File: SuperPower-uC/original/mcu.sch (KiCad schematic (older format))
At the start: 43 parts, among them J7 mcu_pinout, J8 mcu_pinout, Q7 S8050, Q8 S8050, U6 CP2102N-A01-GQFN28, U7 ESP32-WROOM32

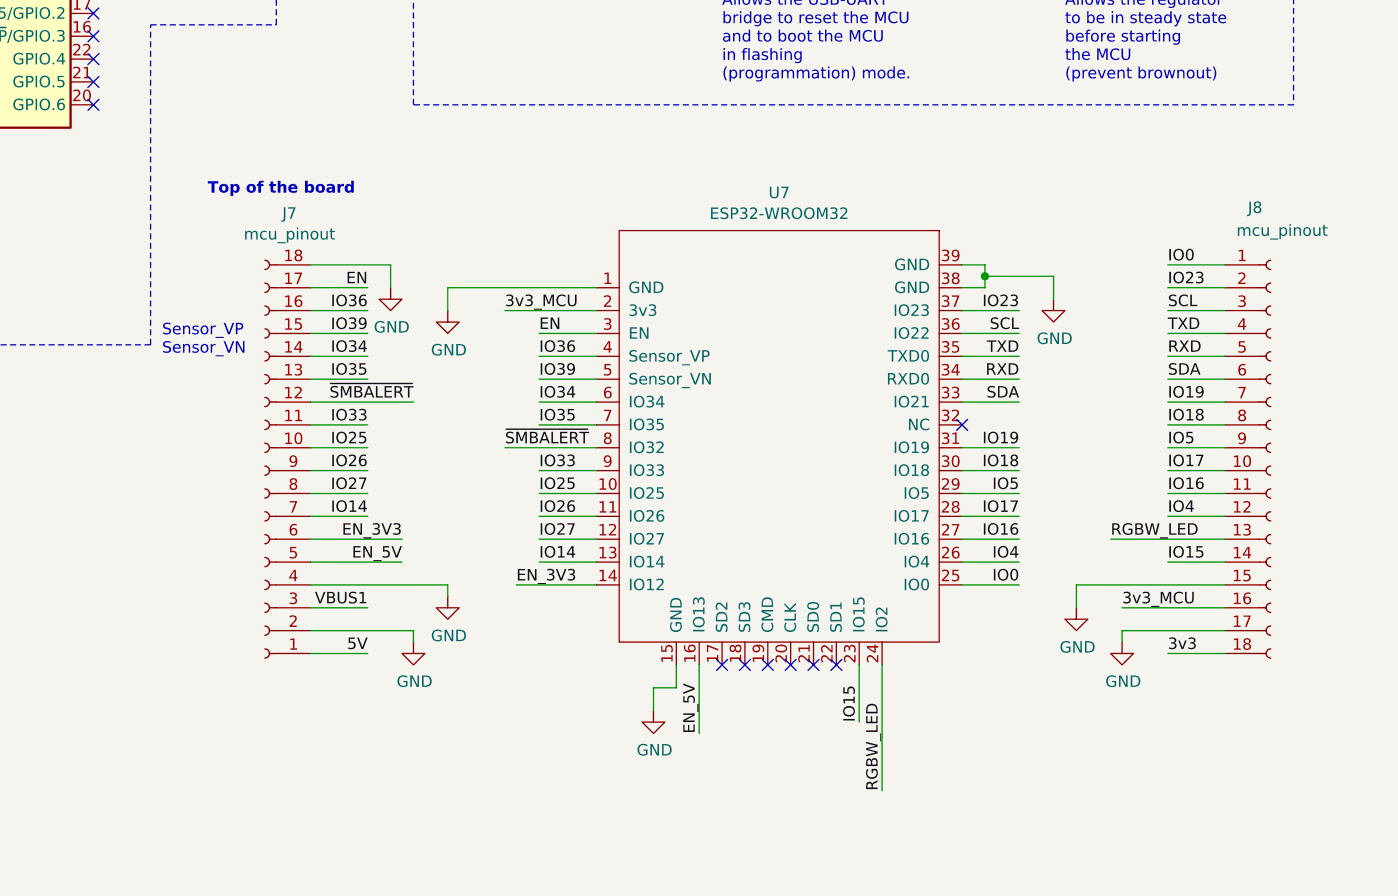
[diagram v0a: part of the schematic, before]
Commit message: Update Single rows Headers to be fully compatible with ESP WROOM modules
(ESP-32 DevKit C rev. 4)
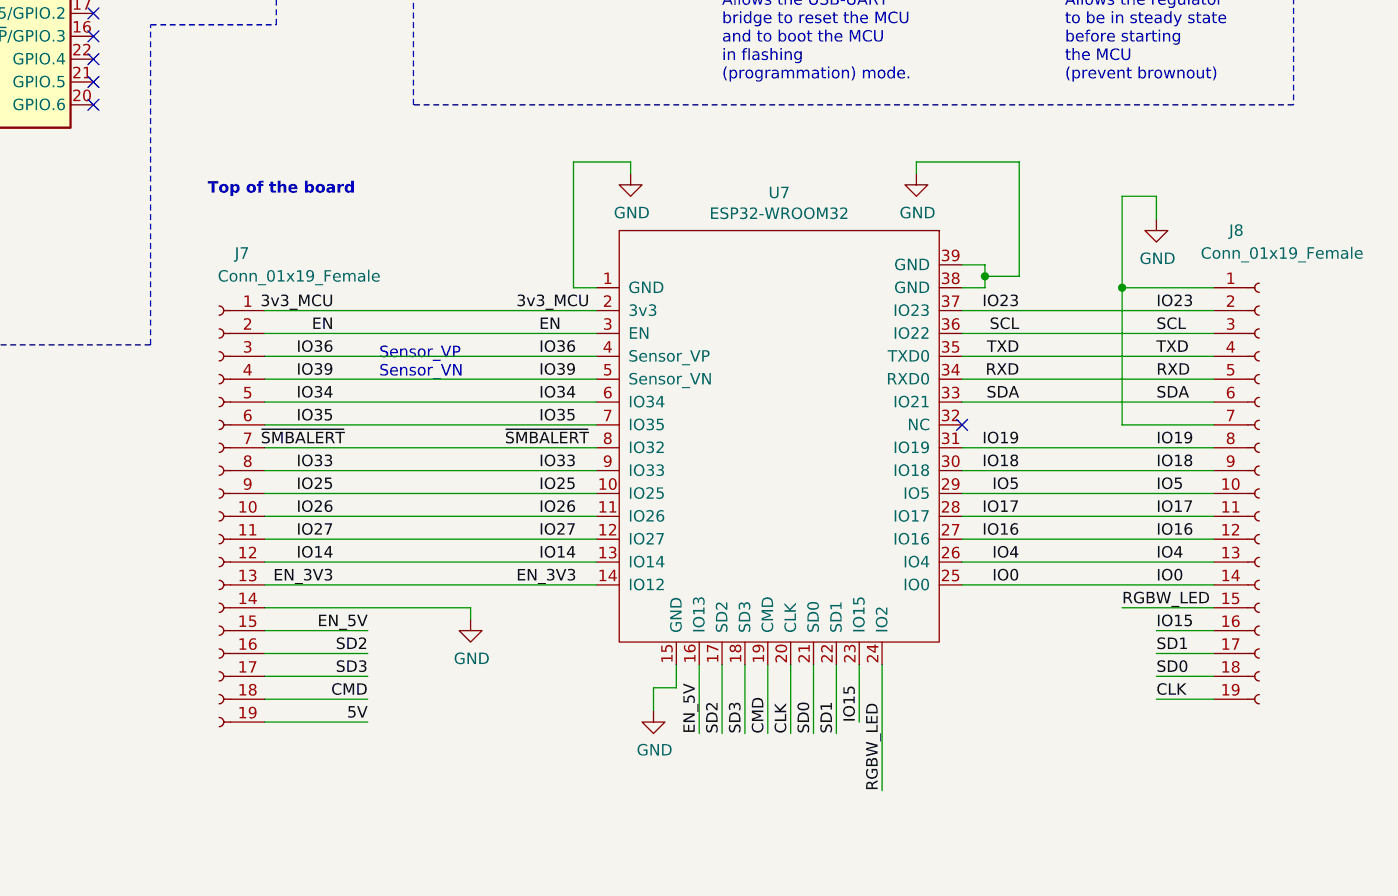
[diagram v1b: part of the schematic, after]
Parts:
- removed J7, J8: mcu_pinout, Connector_PinSocket_2.54mm:PinSocket_1x18_P2.54mm_Vertical, symbol Connector:Conn_01x18_Female
- added J7, J8: Conn_01x19_Female, Connector_PinSocket_2.54mm:PinSocket_1x19_P2.54mm_Vertical, symbol Connector:Conn_01x19_Female
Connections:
- net 3v3_MCU: now also J7.1 (Pin_1)
- net 5V: now also J7.19 (Pin_19)
- net EN: now also J7.2 (Pin_2)
- net EN_3V3: now also J7.13 (Pin_13)
- net EN_5V: now also J7.15 (Pin_15)
- net GND: now also J7.14 (Pin_14), J8.1 (Pin_1), J8.7 (Pin_7)
- net IO0: now also J8.14 (Pin_14)
- net IO14: now also J7.12 (Pin_12)
- net IO15: now also J8.16 (Pin_16)
- net IO16: now also J8.12 (Pin_12)
- net IO17: now also J8.11 (Pin_11)
- net IO18: now also J8.9 (Pin_9)
- net IO19: now also J8.8 (Pin_8)
- net IO23: now also J8.2 (Pin_2)
- net IO25: now also J7.9 (Pin_9)
- net IO26: now also J7.10 (Pin_10)
- net IO27: now also J7.11 (Pin_11)
- net IO33: now also J7.8 (Pin_8)
- net IO34: now also J7.5 (Pin_5)
- net IO35: now also J7.6 (Pin_6)
- net IO36: now also J7.3 (Pin_3)
- net IO39: now also J7.4 (Pin_4)
- net IO4: now also J8.13 (Pin_13)
- net IO5: now also J8.10 (Pin_10)
- net RGBW_LED: now also J8.15 (Pin_15)
- net RXD: now also J8.5 (Pin_5)
- net SCL: now also J8.3 (Pin_3)
- net SDA: now also J8.6 (Pin_6)
- net TXD: now also J8.4 (Pin_4)
- net ~SMBALERT: now also J7.7 (Pin_7)
- net SD2: now reaches U7.17 (SD2)
- net SD2: now also J7.16 (Pin_16)
- net SD3: now reaches U7.18 (SD3)
- net SD3: now also J7.17 (Pin_17)
- net CMD: now reaches U7.19 (CMD)
- net CMD: now also J7.18 (Pin_18)
- net CLK: now reaches U7.20 (CLK)
- net CLK: now also J8.19 (Pin_19)
- net SD0: now reaches U7.21 (SD0)
- net SD0: now also J8.18 (Pin_18)
- net SD1: now reaches U7.22 (SD1)
- net SD1: now also J8.17 (Pin_17)
- no-connect marks 19 -> 13

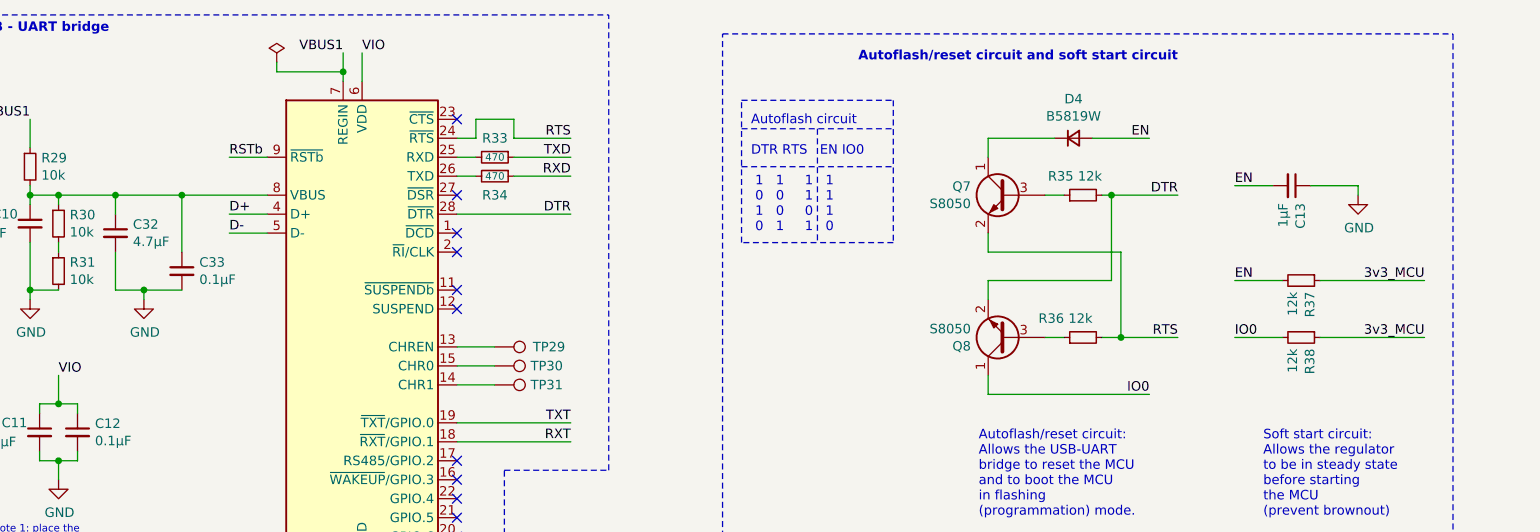
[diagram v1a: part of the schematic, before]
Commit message: Update Placement USB_UART_Bridge
+ Misc.
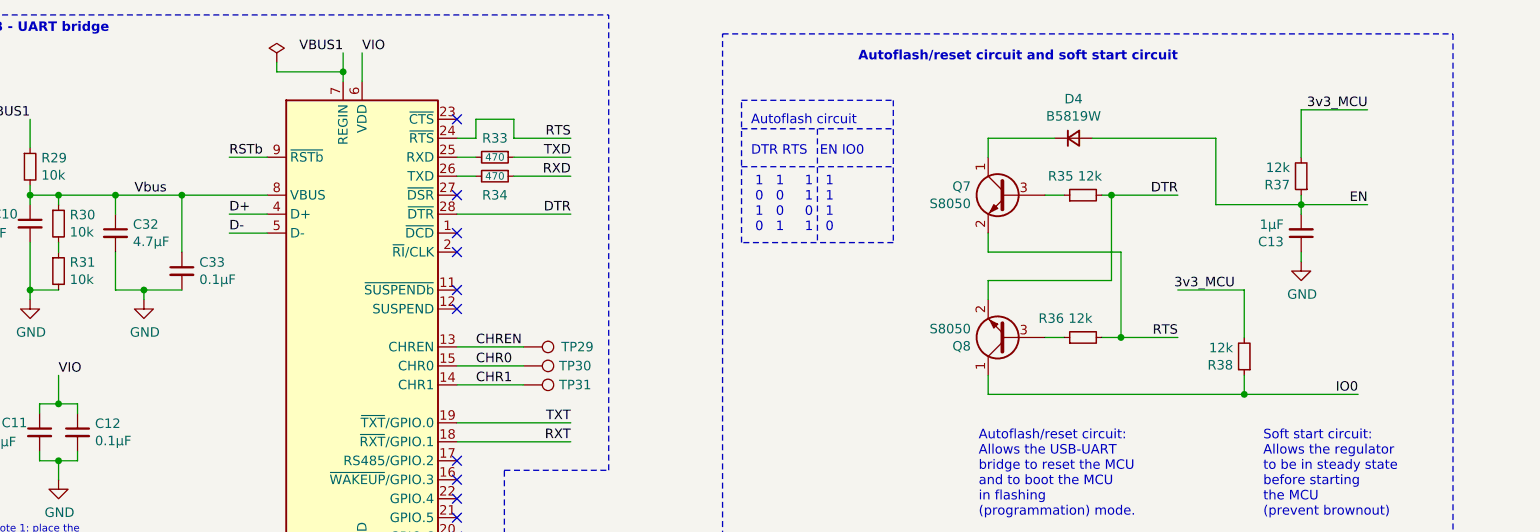
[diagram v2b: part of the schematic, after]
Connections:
- net 3v3_MCU: now also R37.2, R38.2; no longer R37.1, R38.1
- net EN: now also R37.1; no longer R37.2
- net IO0: now also R38.1; no longer R38.2
- net Vbus: now reaches C10.1, C32.1, C33.1, R29.2, R30.1, U6.8 (VBUS)
- net CHREN: now reaches TP29.1, U6.13 (CHREN)
- net CHR0: now reaches TP30.1, U6.15 (CHR0)
- net CHR1: now reaches TP31.1, U6.14 (CHR1)
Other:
- moved on the sheet: C13, R37, R38, TP29, TP30, TP31
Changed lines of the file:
@@
 L Connector:TestPoint TP29
 U 1 1 5FBB75FF
-P 5650 2400
-F 0 "TP29" V 5650 2600 50  0000 L CNN
-F 1 "TestPoint" V 5650 2700 50  0001 L CNN
-F 2 "TestPoint:TestPoint_Pad_D1.0mm" H 5850 2400 50  0001 C CNN
-F 3 "~" H 5850 2400 50  0001 C CNN
-	1    5650 2400
+P 5800 2400
+F 0 "TP29" V 5800 2600 50  0000 L CNN
+F 1 "TestPoint" V 5800 2700 50  0001 L CNN
+F 2 "TestPoint:TestPoint_Pad_D1.0mm" H 6000 2400 50  0001 C CNN
+F 3 "~" H 6000 2400 50  0001 C CNN
+	1    5800 2400
 	0    1    1    0
 $EndComp
@@
 L Connector:TestPoint TP30
 U 1 1 5FBC1FC0
-P 5650 2500
-F 0 "TP30" V 5650 2688 50  0000 L CNN
-F 1 "TestPoint" V 5695 2688 50  0001 L CNN
-F 2 "TestPoint:TestPoint_Pad_D1.0mm" H 5850 2500 50  0001 C CNN
-F 3 "~" H 5850 2500 50  0001 C CNN
-	1    5650 2500
+P 5800 2500
+F 0 "TP30" V 5800 2688 50  0000 L CNN
+F 1 "TestPoint" V 5845 2688 50  0001 L CNN
+F 2 "TestPoint:TestPoint_Pad_D1.0mm" H 6000 2500 50  0001 C CNN
+F 3 "~" H 6000 2500 50  0001 C CNN
+	1    5800 2500
 	0    1    1    0
 $EndComp
@@
 L Connector:TestPoint TP31
 U 1 1 5FBC21DE
-P 5650 2600
-F 0 "TP31" V 5650 2788 50  0000 L CNN
-F 1 "TestPoint" V 5695 2788 50  0001 L CNN
-F 2 "TestPoint:TestPoint_Pad_D1.0mm" H 5850 2600 50  0001 C CNN
-F 3 "~" H 5850 2600 50  0001 C CNN
-	1    5650 2600
-	0    1    1    0
-$EndComp
-Wire Wire Line
-	5650 2400 5450 2400
-Wire Wire Line
-	5450 2500 5650 2500
-Wire Wire Line
-	5650 2600 5450 2600
+P 5800 2600
+F 0 "TP31" V 5800 2788 50  0000 L CNN
+F 1 "TestPoint" V 5845 2788 50  0001 L CNN
+F 2 "TestPoint:TestPoint_Pad_D1.0mm" H 6000 2600 50  0001 C CNN
+F 3 "~" H 6000 2600 50  0001 C CNN
+	1    5800 2600
+	0    1    1    0
+$EndComp
 Text Label 6650 5700 2    50   ~ 0
 EN_5V
@@
 	9250 2350 8950 2350
 Connection ~ 8950 2350
-Wire Wire Line
-	8800 1300 9100 1300
-Text Label 9100 1300 2    50   ~ 0
+Text Label 10250 1650 2    50   ~ 0
 EN
-Wire Wire Line
-	8250 2650 9100 2650
-Text Label 9100 2650 2    50   ~ 0
-IO0
 $Comp
 L power:GND #PWR055
 U 1 1 5F8CBC56
-P 10200 1600
-F 0 "#PWR055" H 10200 1350 50  0001 C CNN
-F 1 "GND" H 10205 1427 50  0000 C CNN
-F 2 "" H 10200 1600 50  0001 C CNN
-F 3 "" H 10200 1600 50  0001 C CNN
-	1    10200 1600
+P 9900 1950
+F 0 "#PWR055" H 9900 1700 50  0001 C CNN
+F 1 "GND" H 9905 1777 50  0000 C CNN
+F 2 "" H 9900 1950 50  0001 C CNN
+F 3 "" H 9900 1950 50  0001 C CNN
+	1    9900 1950
 	1    0    0    -1
 $EndComp
-Text Label 9550 1550 0    50   ~ 0
-EN
-Wire Wire Line
-	9550 1550 9750 1550
+Wire Wire Line
+	9900 1650 9900 1700
 $Comp
 L Device:C_Small C13
 U 1 1 5F8C82E0
-P 9850 1550
-F 0 "C13" H 9942 1596 50  0000 L CNN
-F 1 "1µF" H 9942 1505 50  0000 L CNN
-F 2 "Capacitor_SMD:C_0603_1608Metric" H 9850 1550 50  0001 C CNN
-F 3 "~" H 9850 1550 50  0001 C CNN
-	1    9850 1550
-	0    1    1    0
-$EndComp
-Text Label 9550 2050 0    50   ~ 0
-EN
+P 9900 1800
+F 0 "C13" H 9992 1846 50  0000 L CNN
+F 1 "1µF" H 9992 1755 50  0000 L CNN
+F 2 "Capacitor_SMD:C_0603_1608Metric" H 9900 1800 50  0001 C CNN
+F 3 "~" H 9900 1800 50  0001 C CNN
+	1    9900 1800
+	-1   0    0    1
+$EndComp
 $Comp
 L Device:R_Small R37
 U 1 1 5FE5C5F7
-P 9900 2050
-F 0 "R37" H 9959 2096 50  0000 L CNN
-F 1 "12k" H 9959 2005 50  0000 L CNN
-F 2 "Resistor_SMD:R_0603_1608Metric" H 9900 2050 50  0001 C CNN
-F 3 "~" H 9900 2050 50  0001 C CNN
-	1    9900 2050
-	0    1    1    0
-$EndComp
-Text Label 10550 2050 2    50   ~ 0
+P 9900 1500
+F 0 "R37" H 9959 1546 50  0000 L CNN
+F 1 "12k" H 9959 1455 50  0000 L CNN
+F 2 "Resistor_SMD:R_0603_1608Metric" H 9900 1500 50  0001 C CNN
+F 3 "~" H 9900 1500 50  0001 C CNN
+	1    9900 1500
+	-1   0    0    1
+$EndComp
+Text Label 10250 1150 2    50   ~ 0
 3v3_MCU
-Wire Wire Line
-	9550 2050 9800 2050
-Wire Wire Line
-	10000 2050 10550 2050
 $Comp
 L Device:R_Small R38
 U 1 1 5FE7288F
-P 9900 2350
-F 0 "R38" H 9959 2396 50  0000 L CNN
-F 1 "12k" H 9959 2305 50  0000 L CNN
-F 2 "Resistor_SMD:R_0603_1608Metric" H 9900 2350 50  0001 C CNN
-F 3 "~" H 9900 2350 50  0001 C CNN
-	1    9900 2350
-	0    1    1    0
-$EndComp
-Text Label 10550 2350 2    50   ~ 0
+P 9600 2450
+F 0 "R38" H 9659 2496 50  0000 L CNN
+F 1 "12k" H 9659 2405 50  0000 L CNN
+F 2 "Resistor_SMD:R_0603_1608Metric" H 9600 2450 50  0001 C CNN
+F 3 "~" H 9600 2450 50  0001 C CNN
+	1    9600 2450
+	-1   0    0    1
+$EndComp
+Text Label 9550 2100 2    50   ~ 0
 3v3_MCU
-Wire Wire Line
-	9550 2350 9800 2350
-Wire Wire Line
-	10000 2350 10550 2350
-Text Label 9550 2350 0    50   ~ 0
+Text Label 10200 2650 2    50   ~ 0
 IO0
 Wire Wire Line
-	10200 1600 10200 1550
-Wire Wire Line
-	10200 1550 9950 1550
+	9900 1950 9900 1900
 Text Notes 8200 3300 0    50   ~ 0
 Autoflash/reset circuit:\nAllows the USB-UART\nbridge to reset the MCU\nand to boot the MCU\nin flashing\n(programmation) mode.
@@
 Wire Wire Line
 	9250 4300 10350 4300
+Wire Wire Line
+	5450 2600 5800 2600
+Wire Wire Line
+	5450 2500 5800 2500
+Wire Wire Line
+	5450 2400 5800 2400
+Text Label 5550 2400 0    50   ~ 0
+CHREN
+Text Label 5550 2500 0    50   ~ 0
+CHR0
+Text Label 5550 2600 0    50   ~ 0
+CHR1
+Text Label 3750 1600 0    50   ~ 0
+Vbus
+Wire Wire Line
+	9450 1300 9450 1650
+Wire Wire Line
+	9450 1650 9900 1650
+Wire Wire Line
+	8800 1300 9450 1300
+Wire Wire Line
+	9900 1600 9900 1650
+Connection ~ 9900 1650
+Wire Wire Line
+	9900 1400 9900 1150
+Wire Wire Line
+	9900 1150 10250 1150
+Wire Wire Line
+	9600 2350 9600 2100
+Wire Wire Line
+	9600 2100 9250 2100
+Wire Wire Line
+	9600 2650 9600 2550
+Wire Wire Line
+	8250 2650 9600 2650
+Wire Wire Line
+	9600 2650 10200 2650
+Connection ~ 9600 2650
+Wire Wire Line
+	9900 1650 10250 1650
 $EndSCHEMATC
